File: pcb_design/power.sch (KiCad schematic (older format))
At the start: 40 parts, among them Q1 BSC340N08, Q3 AO4805, U11 LM3488, U13 LM1117IMP-v.v, U9 LM22676QTJ-5.0

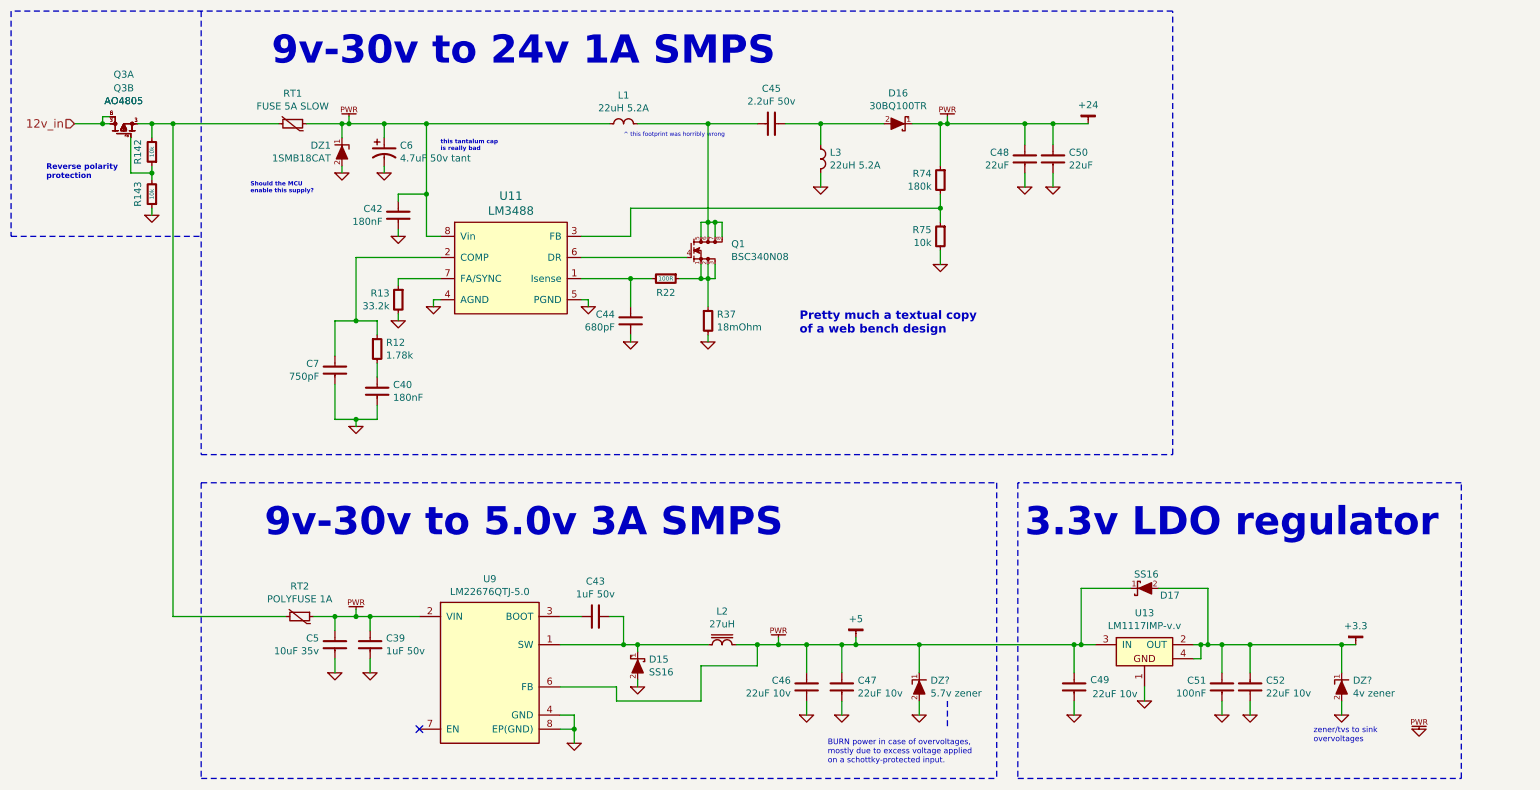
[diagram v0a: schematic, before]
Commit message: Fixed power supply inductor footprints in the layout
Signed-off-by: Marcos Chaparro <mchaparro@paltatech.com>
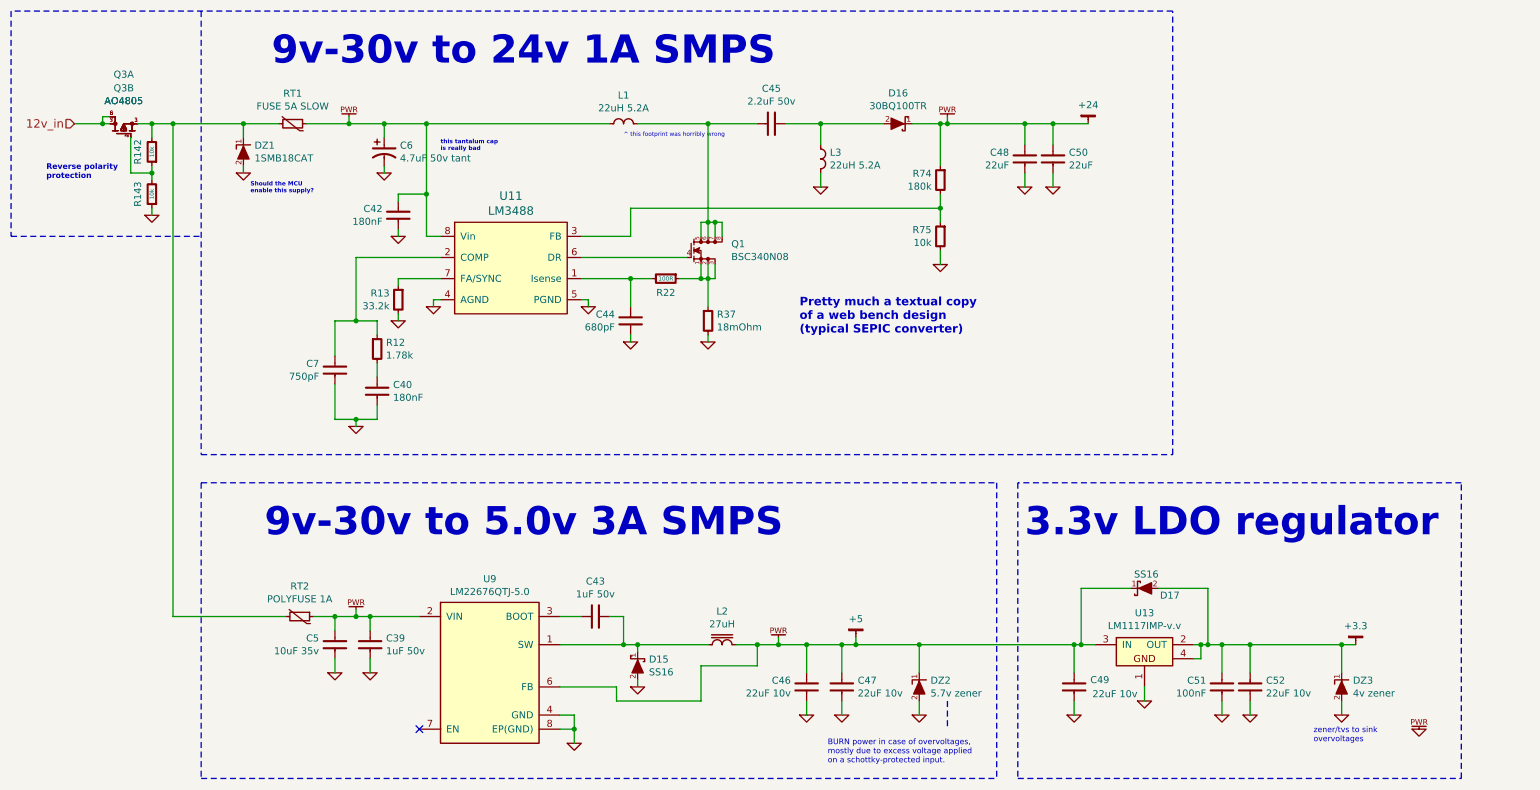
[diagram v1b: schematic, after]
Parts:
- gave numbers to parts that had none: 2
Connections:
- net at C42.1, C6.1, L1.2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: no longer DZ1.1 (K)
- net at Q3.1 (S2), Q3.3 (S1), R142.2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: now also DZ1.1 (K)
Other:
- note added: "Pretty much a textual copy\nof a web bench design\n(typical SEPIC converter)"
- note removed: "Pretty much a textual copy\nof a web bench design"
- moved on the sheet: DZ1

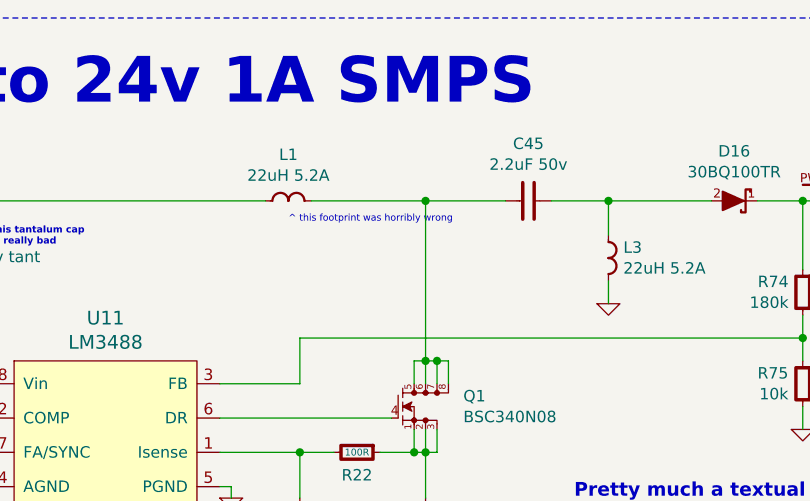
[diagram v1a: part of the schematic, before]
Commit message: Added RC filter to FAULT line to prevent noise triggering it
Signed-off-by: Marcos Chaparro <mchaparro@paltatech.com>
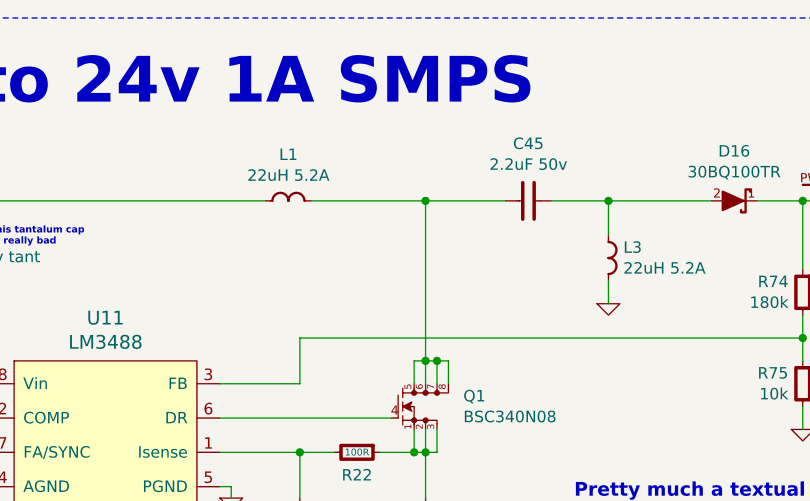
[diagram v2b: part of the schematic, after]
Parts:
- C42: BOM CAP MLCC 100pF C0G 50V 5% [0603] -> CAP MLCC 180nF X7R 50V 5% [0603]
- C51: BOM CAP MLCC 100pF C0G 50V 5% [0603] -> CAP MLCC 100nF C0G 50V 5% [0603]
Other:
- note removed: "^ this footprint was horribly wrong"
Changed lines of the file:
@@
 F 2 "IPC7351-Nominal:CAPC1608X55" H 3300 2700 50  0001 C CNN
 F 3 "http://www.murata.com/~/media/webrenewal/support/library/catalog/products/capacitor/mlcc/c02e.ashx" H 3290 2675 60  0001 C CNN
-F 4 "CAP MLCC 100pF C0G 50V 5% [0603]" H 4100 3250 60  0001 C CNN "BOM"
+F 4 "CAP MLCC 180nF X7R 50V 5% [0603]" H 4100 3250 60  0001 C CNN "BOM"
 F 5 "Murata Electronics North America" H 0   0   50  0001 C CNN "MFR"
 F 6 "GRM188R71E184KA88D" H 0   0   50  0001 C CNN "MPN"
@@
 F 2 "IPC7351-Nominal:CAPC1608X55" H 9150 6050 50  0001 C CNN
 F 3 "http://www.murata.com/~/media/webrenewal/support/library/catalog/products/capacitor/mlcc/c02e.ashx" H 9140 6025 60  0001 C CNN
-F 4 "CAP MLCC 100pF C0G 50V 5% [0603]" H 9950 6600 60  0001 C CNN "BOM"
+F 4 "CAP MLCC 100nF C0G 50V 5% [0603]" H 9950 6600 60  0001 C CNN "BOM"
 F 5 "Murata Electronics North America" H 200 0   50  0001 C CNN "MFR"
 F 6 "GRM188R71E104KA01D" H 200 0   50  0001 C CNN "MPN"
@@
 Connection ~ 1550 2400
 NoConn ~ 3450 6350
-Text Notes 4900 2150 0    30   ~ 0
-^ this footprint was horribly wrong
 $Comp
 L 1SMA59xxBT3G DZ3
